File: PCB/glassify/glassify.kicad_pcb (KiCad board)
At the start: 2 copper layers, 61 x 58 mm, 16 parts, among them J1 Conn_02x09_Odd_Even

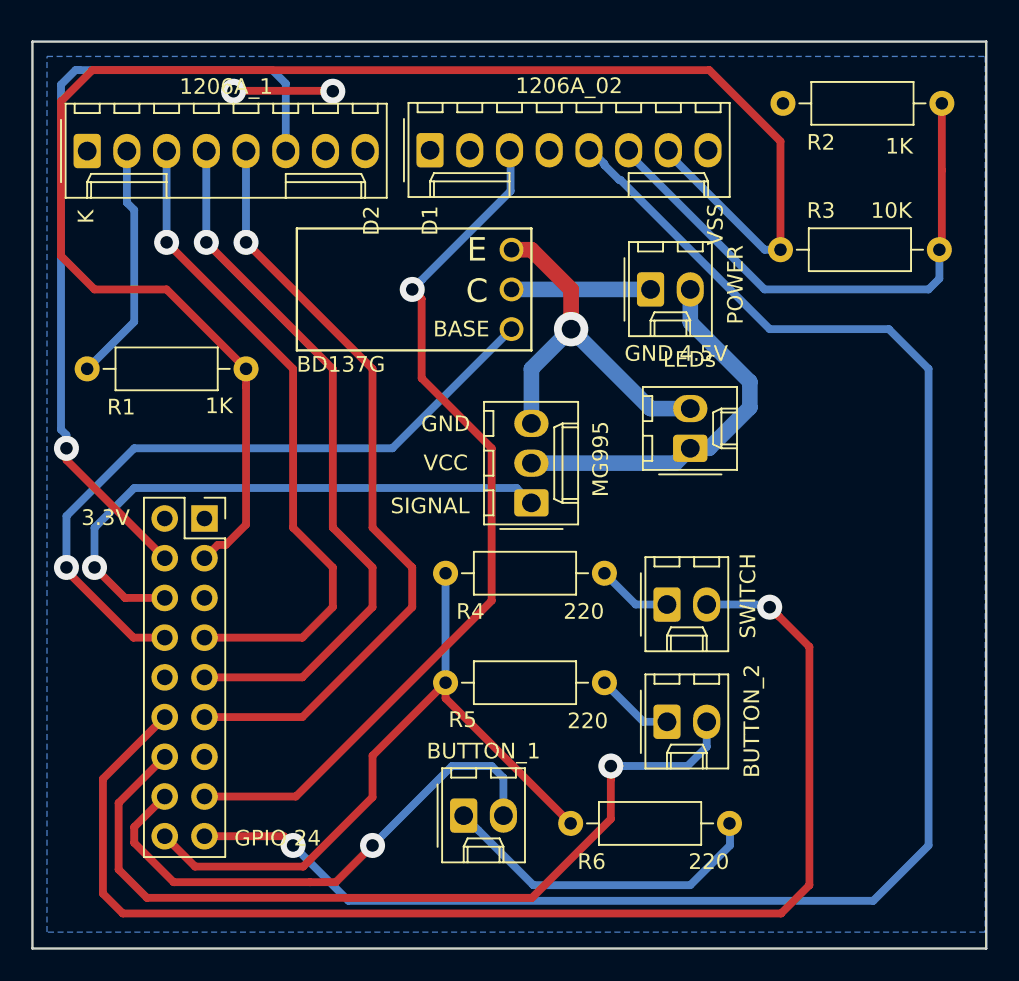
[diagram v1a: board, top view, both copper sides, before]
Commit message: Added LEDs to have the option of installing more if needed, fixed ground layer on main board to be connected everywhere, rewired pins to ease soldering
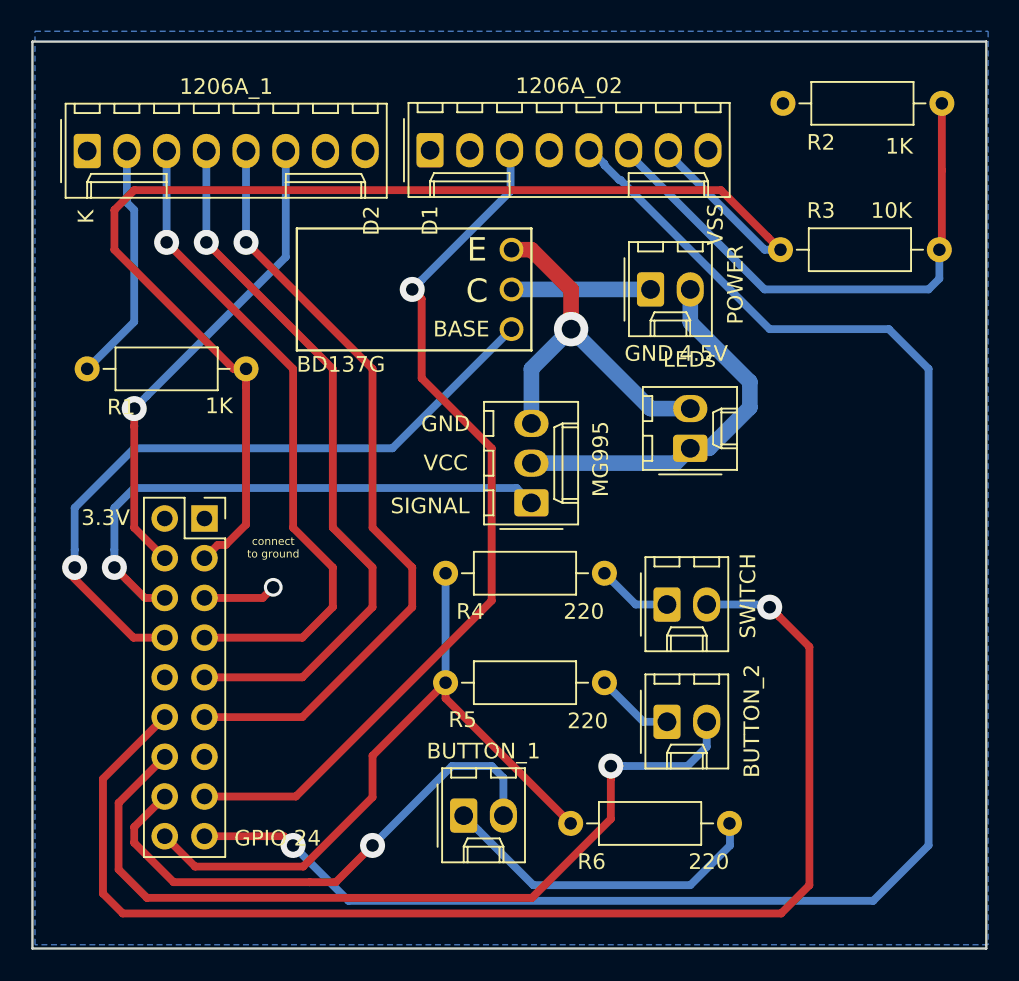
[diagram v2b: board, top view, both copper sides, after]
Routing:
- net Net-(1206A_01x08_Male1-Pad6): track 52.5 -> 30.9 mm
- net Net-(1206A_01x08_Male2-Pad7): track 103.7 -> 82.2 mm
- net (no net): track 6.39 -> 0.00 mm, vias 2 -> 0
- net Net-(1206A_01x08_Male1-Pad1): track 0.00 -> 4.68 mm, vias 0 -> 1
- net Net-(2mm_pitch4-Pad1): track 37.2 -> 35.4 mm
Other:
- net class Default: trace_width 1 -> 0.5
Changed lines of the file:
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@@
   (general
     (thickness 1.6)
-    (drawings 21)
-    (tracks 178)
+    (drawings 22)
+    (tracks 174)
     (zones 0)
     (modules 16)
@@
   )
   (setup
-    (last_trace_width 1)
+    (last_trace_width 0.5)
     (trace_clearance 0.5)
     (zone_clearance 0.508)
@@
   (net_class Default "This is the default net class."
     (clearance 0.5)
-    (trace_width 1)
+    (trace_width 0.5)
     (via_dia 1.2)
     (via_drill 0.8)
@@
     )
   )
+  (gr_text "connect\nto ground" (at 140.97 105.41) (layer F.SilkS)
+    (effects (font (size 0.5 0.5) (thickness 0.125)))
+  )
   (gr_text "connect to ground" (at 142.24 109.22) (layer B.SilkS)
     (effects (font (size 0.5 0.5) (thickness 0.125)))
@@
   (gr_line (start 186.57 131.05) (end 125.57 131.05) (layer Edge.Cuts) (width 0.15))
   (gr_line (start 186.57 73.05) (end 186.57 131.05) (layer Edge.Cuts) (width 0.15))
-  (via (at 144.78 76.22501) (size 1.6) (drill 0.8) (layers F.Cu B.Cu) (net 0))
-  (segment (start 138.43 76.2) (end 144.75499 76.2) (width 0.5) (layer F.Cu) (net 0))
-  (segment (start 144.75499 76.2) (end 144.78 76.22501) (width 0.5) (layer F.Cu) (net 0))
-  (via (at 138.43 76.22501) (size 1.6) (drill 0.8) (layers F.Cu B.Cu) (net 0))
-  (segment (start 138.43 76.2) (end 138.43 76.22501) (width 0.5) (layer F.Cu) (net 0))
+  (via (at 140.97 107.95) (size 1.2) (drill 0.8) (layers F.Cu B.Cu) (net 1))
+  (segment (start 136.57 108.63) (end 140.29 108.63) (width 0.5) (layer F.Cu) (net 1))
+  (segment (start 140.29 108.63) (end 140.97 107.95) (width 0.5) (layer F.Cu) (net 1))
   (segment (start 132.08 90.97) (end 129.07 93.98) (width 0.5) (layer B.Cu) (net 2))
   (segment (start 132.08 83.82) (end 132.08 90.97) (width 0.5) (layer B.Cu) (net 2))
@@
   (via (at 139.23 85.89) (size 1.6) (drill 0.8) (layers F.Cu B.Cu) (net 5))
   (segment (start 134.029978 106.09) (end 134.03 106.09) (width 0.5) (layer B.Cu) (net 6))
-  (segment (start 134.03 106.09) (end 127.745 99.805) (width 0.5) (layer F.Cu) (net 6))
-  (via (at 127.745 99.06) (size 1.6) (drill 0.8) (layers F.Cu B.Cu) (net 6))
-  (segment (start 127.745 99.805) (end 127.745 99.06) (width 0.5) (layer F.Cu) (net 6))
-  (segment (start 127.39501 97.861482) (end 127.39501 75.80499) (width 0.5) (layer B.Cu) (net 6))
-  (segment (start 127.745 99.06) (end 127.745 98.211472) (width 0.5) (layer B.Cu) (net 6))
-  (segment (start 127.745 98.211472) (end 127.39501 97.861482) (width 0.5) (layer B.Cu) (net 6))
-  (segment (start 128.32499 74.87501) (end 128.57499 74.87501) (width 0.5) (layer B.Cu) (net 6))
-  (segment (start 127.39501 75.80499) (end 128.32499 74.87501) (width 0.5) (layer B.Cu) (net 6))
-  (segment (start 140.91501 74.87501) (end 128.57499 74.87501) (width 0.5) (layer B.Cu) (net 6))
-  (segment (start 141.77 80.05) (end 141.77 75.73) (width 0.5) (layer B.Cu) (net 6))
-  (segment (start 141.77 75.73) (end 140.91501 74.87501) (width 0.5) (layer B.Cu) (net 6))
+  (via (at 132.079992 96.52) (size 1.6) (drill 0.8) (layers F.Cu B.Cu) (net 6))
+  (segment (start 141.77 86.829992) (end 132.879991 95.720001) (width 0.5) (layer B.Cu) (net 6))
+  (segment (start 132.879991 95.720001) (end 132.079992 96.52) (width 0.5) (layer B.Cu) (net 6))
+  (segment (start 141.77 80.05) (end 141.77 86.829992) (width 0.5) (layer B.Cu) (net 6))
+  (segment (start 132.079992 97.65137) (end 132.079992 96.52) (width 0.5) (layer F.Cu) (net 6))
+  (segment (start 132.079992 104.139992) (end 132.079992 97.65137) (width 0.5) (layer F.Cu) (net 6))
+  (segment (start 134.03 106.09) (end 132.079992 104.139992) (width 0.5) (layer F.Cu) (net 6))
   (segment (start 172.72 86.36) (end 173.41 86.36) (width 0.5) (layer B.Cu) (net 9))
   (segment (start 172.39 86.36) (end 172.72 86.36) (width 0.5) (layer B.Cu) (net 9))
@@
   (segment (start 137.930001 105.240001) (end 139.23 103.940002) (width 0.5) (layer F.Cu) (net 9))
   (segment (start 136.57 106.09) (end 137.419999 105.240001) (width 0.5) (layer F.Cu) (net 9))
-  (segment (start 134.15 88.9) (end 139.23 93.98) (width 0.5) (layer F.Cu) (net 9))
-  (segment (start 173.41 79.43) (end 168.85501 74.87501) (width 0.5) (layer F.Cu) (net 9))
-  (segment (start 168.85501 74.87501) (end 129.400392 74.87501) (width 0.5) (layer F.Cu) (net 9))
-  (segment (start 129.54 88.9) (end 134.15 88.9) (width 0.5) (layer F.Cu) (net 9))
-  (segment (start 127.39501 76.880392) (end 127.39501 86.75501) (width 0.5) (layer F.Cu) (net 9))
-  (segment (start 129.400392 74.87501) (end 127.39501 76.880392) (width 0.5) (layer F.Cu) (net 9))
-  (segment (start 173.41 86.36) (end 173.41 79.43) (width 0.5) (layer F.Cu) (net 9))
-  (segment (start 127.39501 86.75501) (end 129.54 88.9) (width 0.5) (layer F.Cu) (net 9))
+  (segment (start 172.610001 85.560001) (end 173.41 86.36) (width 0.5) (layer F.Cu) (net 9))
+  (segment (start 132.08 82.55) (end 169.6 82.55) (width 0.5) (layer F.Cu) (net 9))
+  (segment (start 169.6 82.55) (end 172.610001 85.560001) (width 0.5) (layer F.Cu) (net 9))
+  (segment (start 138.43 93.98) (end 130.81 86.36) (width 0.5) (layer F.Cu) (net 9))
+  (segment (start 139.23 93.98) (end 138.43 93.98) (width 0.5) (layer F.Cu) (net 9))
+  (segment (start 130.81 86.36) (end 130.81 83.82) (width 0.5) (layer F.Cu) (net 9))
+  (segment (start 130.81 83.82) (end 132.08 82.55) (width 0.5) (layer F.Cu) (net 9))
   (segment (start 183.73 86.2) (end 183.57 86.36) (width 0.5) (layer F.Cu) (net 10))
   (segment (start 183.73 77) (end 183.73 81.28) (width 0.5) (layer F.Cu) (net 10))
@@
   (segment (start 170.18 124.46) (end 167.64 127) (width 0.5) (layer B.Cu) (net 20))
   (segment (start 170.18 123.08) (end 170.18 124.46) (width 0.5) (layer B.Cu) (net 20))
-  (via (at 129.54 106.68) (size 1.6) (drill 0.8) (layers F.Cu B.Cu) (net 21))
-  (segment (start 134.03 108.63) (end 131.49 108.63) (width 0.5) (layer F.Cu) (net 21))
-  (segment (start 131.49 108.63) (end 129.54 106.68) (width 0.5) (layer F.Cu) (net 21))
   (segment (start 156.53 101.6) (end 156.540227 101.610227) (width 0.5) (layer B.Cu) (net 21))
-  (segment (start 132.08 101.6) (end 156.53 101.6) (width 0.5) (layer B.Cu) (net 21))
-  (segment (start 129.54 106.68) (end 129.54 104.14) (width 0.5) (layer B.Cu) (net 21))
-  (segment (start 129.54 104.14) (end 132.08 101.6) (width 0.5) (layer B.Cu) (net 21))
   (segment (start 156.53 101.6) (end 157.48 102.55) (width 0.5) (layer B.Cu) (net 21))
+  (segment (start 132.08 101.6) (end 130.81 102.87) (width 0.5) (layer B.Cu) (net 21))
+  (segment (start 156.53 101.6) (end 132.08 101.6) (width 0.5) (layer B.Cu) (net 21))
+  (segment (start 131.609999 107.479999) (end 130.81 106.68) (width 0.5) (layer F.Cu) (net 21))
+  (segment (start 130.81 102.87) (end 130.81 105.54863) (width 0.5) (layer B.Cu) (net 21))
+  (segment (start 134.03 108.63) (end 132.76 108.63) (width 0.5) (layer F.Cu) (net 21))
+  (segment (start 130.81 105.54863) (end 130.81 106.68) (width 0.5) (layer B.Cu) (net 21))
+  (segment (start 132.76 108.63) (end 131.609999 107.479999) (width 0.5) (layer F.Cu) (net 21))
+  (via (at 130.81 106.68) (size 1.6) (drill 0.8) (layers F.Cu B.Cu) (net 21))
   (segment (start 167.64 91) (end 171.45 94.81) (width 1) (layer B.Cu) (net 22))
   (segment (start 167.64 88.9) (end 167.64 91) (width 1) (layer B.Cu) (net 22))
@@
   (segment (start 157.48 86.36) (end 160.02 88.9) (width 1) (layer F.Cu) (net 23))
   (segment (start 160.02 88.9) (end 160.02 91.44) (width 1) (layer F.Cu) (net 23))
-  (via (at 160.02 91.44) (size 2.2) (drill 1.2) (layers F.Cu B.Cu) (net 23) (status 1000000))
+  (via (at 160.02 91.44) (size 2.2) (drill 1.2) (layers F.Cu B.Cu) (net 23))
   (segment (start 167.64 96.52) (end 165.1 96.52) (width 1) (layer B.Cu) (net 23))
   (segment (start 165.1 96.52) (end 160.02 91.44) (width 1) (layer B.Cu) (net 23))
@@
   (segment (start 157.48 97.47) (end 157.48 93.98) (width 1) (layer B.Cu) (net 23))
   (segment (start 165.1 88.9) (end 156.540001 88.9) (width 1) (layer B.Cu) (net 24))
-  (via (at 127.745 106.68) (size 1.6) (drill 0.8) (layers F.Cu B.Cu) (net 25))
   (segment (start 134.03 111.17) (end 132.031998 111.17) (width 0.5) (layer F.Cu) (net 25))
-  (segment (start 148.59 99.06) (end 156.21 91.44) (width 0.5) (layer B.Cu) (net 25))
-  (segment (start 132.08 99.06) (end 148.59 99.06) (width 0.5) (layer B.Cu) (net 25))
-  (segment (start 127.745 103.395) (end 132.08 99.06) (width 0.5) (layer B.Cu) (net 25))
   (segment (start 132.031998 111.17) (end 127.745 106.883002) (width 0.5) (layer F.Cu) (net 25))
-  (segment (start 127.745 106.68) (end 127.745 103.395) (width 0.5) (layer B.Cu) (net 25))
+  (segment (start 128.27 102.87) (end 128.27 105.54863) (width 0.5) (layer B.Cu) (net 25))
+  (segment (start 128.27 105.54863) (end 128.27 106.68) (width 0.5) (layer B.Cu) (net 25))
+  (segment (start 132.08 99.06) (end 128.27 102.87) (width 0.5) (layer B.Cu) (net 25))
+  (segment (start 148.59 99.06) (end 132.08 99.06) (width 0.5) (layer B.Cu) (net 25))
+  (via (at 128.27 106.68) (size 1.6) (drill 0.8) (layers F.Cu B.Cu) (net 25))
+  (segment (start 156.21 91.44) (end 148.59 99.06) (width 0.5) (layer B.Cu) (net 25))
   (segment (start 142.888015 125.810001) (end 147.32 121.378016) (width 0.5) (layer F.Cu) (net 26))
   (segment (start 134.03 123.87) (end 135.970001 125.810001) (width 0.5) (layer F.Cu) (net 26))
@@
     (polygon
       (pts
-        (xy 186.5 74) (xy 186.5 130) (xy 126.5 130) (xy 126.5 74)
+        (xy 186.69 72.39) (xy 186.69 130.81) (xy 125.73 130.81) (xy 125.73 72.39)
       )
     )
